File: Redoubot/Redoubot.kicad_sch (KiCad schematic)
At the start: 4 parts, among them U1 STM32G431RBTx, Y1 8MHz

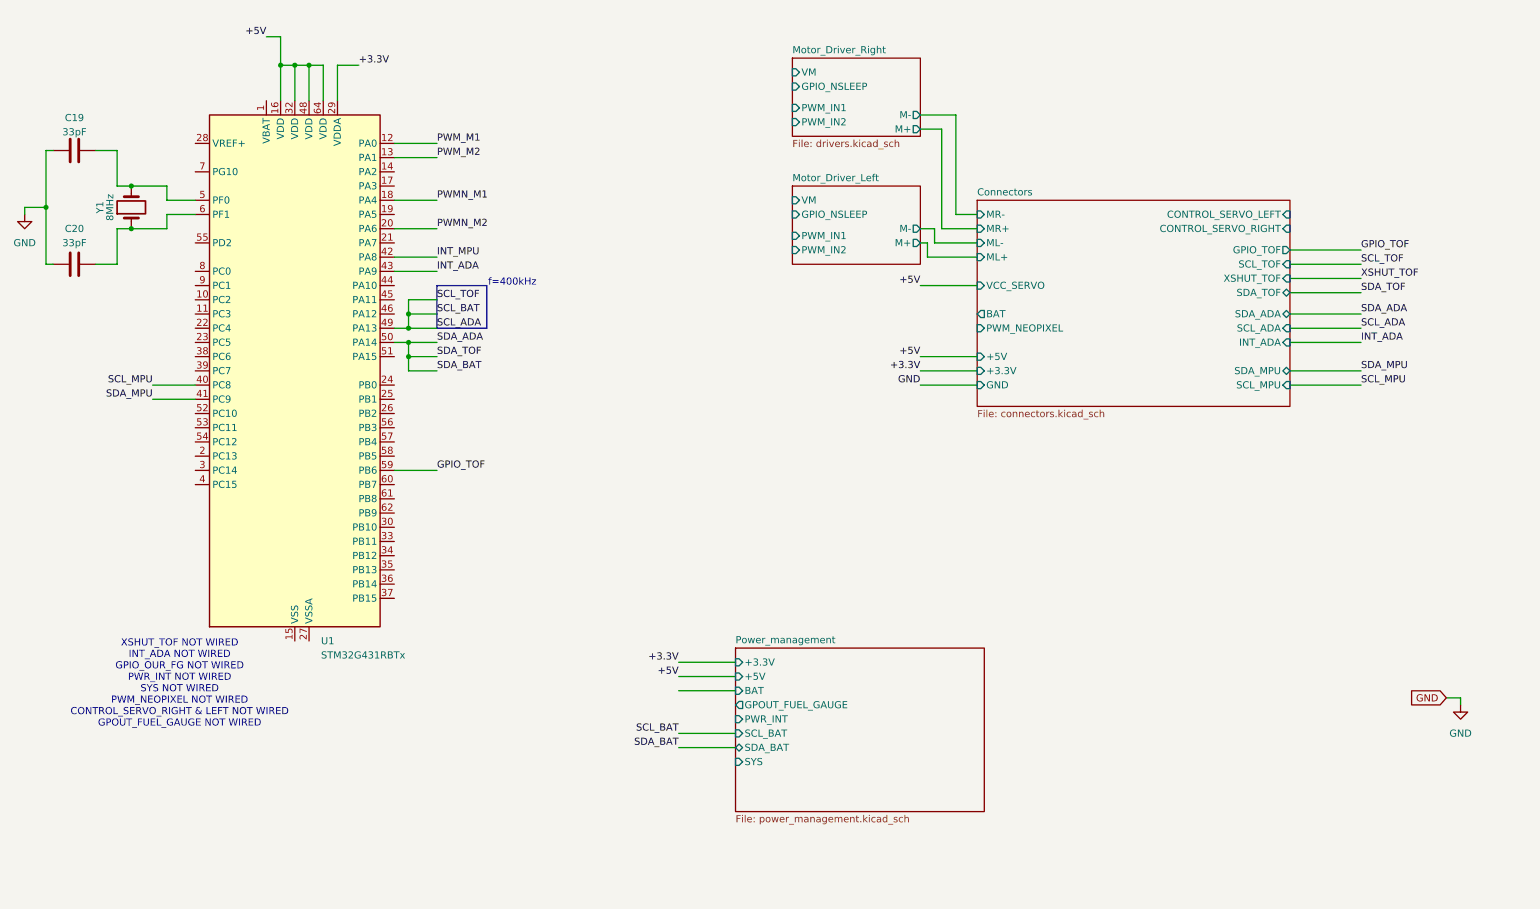
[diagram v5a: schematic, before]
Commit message: feat: added DFPlayer Mini and HM10 connectors
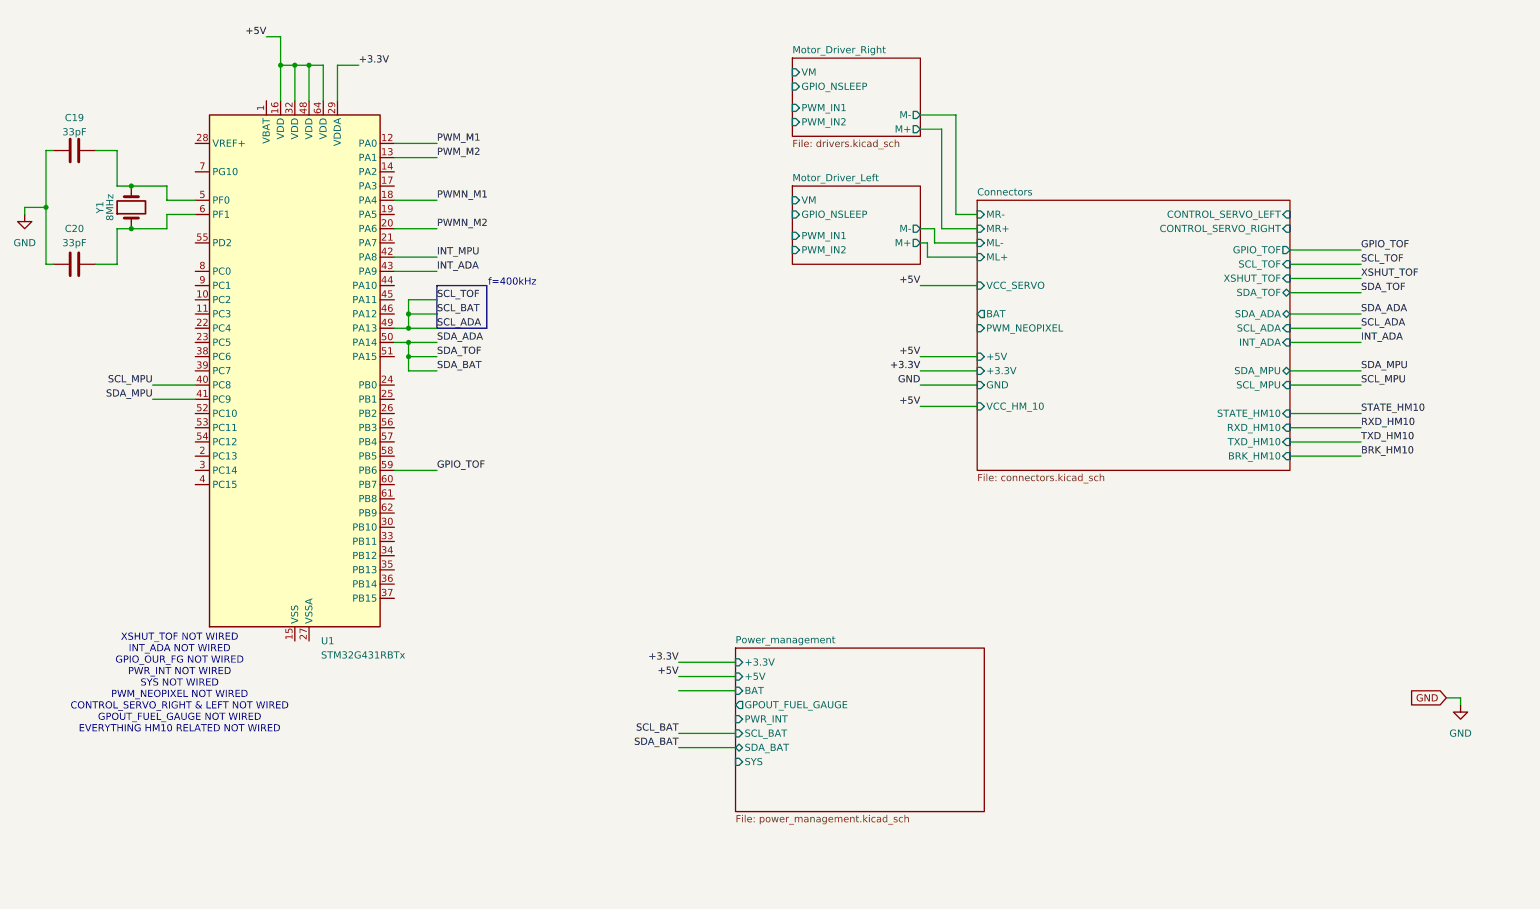
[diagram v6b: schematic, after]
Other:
- sheet Connectors ports: added BRK_HM10, RXD_HM10, STATE_HM10, TXD_HM10, VCC_HM_10; removed none
- note added: "XSHUT_TOF NOT WIRED INT_ADA NOT WIRED GPIO_OUR_FG NOT WIRED PWR_INT NOT WIRED SYS NOT WIRED PWM_NEOPIXEL NOT WIRED CONTROL_SERVO_RIGHT & LEFT NOT WIRED GPOUT_FUEL_GAUGE NOT WIRED EVERYTHING HM10 RELATED NOT WIRED"
- note removed: "XSHUT_TOF NOT WIRED INT_ADA NOT WIRED GPIO_OUR_FG NOT WIRED PWR_INT NOT WIRED SYS NOT WIRED PWM_NEOPIXEL NOT WIRED CONTROL_SERVO_RIGHT & LEFT NOT WIRED GPOUT_FUEL_GAUGE NOT WIRED"
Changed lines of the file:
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@@
 		)
 	)
-	(text "XSHUT_TOF NOT WIRED\nINT_ADA NOT WIRED\nGPIO_OUR_FG NOT WIRED\nPWR_INT NOT WIRED\nSYS NOT WIRED\nPWM_NEOPIXEL NOT WIRED\nCONTROL_SERVO_RIGHT & LEFT NOT WIRED\nGPOUT_FUEL_GAUGE NOT WIRED"
+	(text "XSHUT_TOF NOT WIRED\nINT_ADA NOT WIRED\nGPIO_OUR_FG NOT WIRED\nPWR_INT NOT WIRED\nSYS NOT WIRED\nPWM_NEOPIXEL NOT WIRED\nCONTROL_SERVO_RIGHT & LEFT NOT WIRED\nGPOUT_FUEL_GAUGE NOT WIRED\nEVERYTHING HM10 RELATED NOT WIRED\n"
 		(exclude_from_sim no)
 		(at 42.926 134.62 0)
@@
 	(wire
 		(pts
+			(xy 175.26 85.09) (xy 185.42 85.09)
+		)
+		(stroke
+			(width 0)
+			(type default)
+		)
+	)
+	(wire
+		(pts
+			(xy 241.3 86.36) (xy 254 86.36)
+		)
+		(stroke
+			(width 0)
+			(type default)
+		)
+	)
+	(wire
+		(pts
 			(xy 241.3 62.23) (xy 254 62.23)
 		)
@@
 	(wire
 		(pts
+			(xy 241.3 91.44) (xy 254 91.44)
+		)
+		(stroke
+			(width 0)
+			(type default)
+		)
+	)
+	(wire
+		(pts
 			(xy 241.3 68.58) (xy 254 68.58)
 		)
@@
 	(wire
 		(pts
+			(xy 241.3 93.98) (xy 254 93.98)
+		)
+		(stroke
+			(width 0)
+			(type default)
+		)
+	)
+	(wire
+		(pts
 			(xy 83.82 71.12) (xy 81.28 71.12)
 		)
@@
 		(pts
 			(xy 31.75 45.72) (xy 31.75 39.37)
+		)
+		(stroke
+			(width 0)
+			(type default)
+		)
+	)
+	(wire
+		(pts
+			(xy 241.3 88.9) (xy 254 88.9)
 		)
 		(stroke
@@
 		)
 	)
+	(label "TXD_HM10"
+		(at 254 91.44 0)
+		(effects
+			(font
+				(size 1.27 1.27)
+			)
+			(justify left bottom)
+		)
+	)
 	(label "SDA_ADA"
 		(at 88.9 73.66 0)
@@
 	)
 	(label "+5V"
+		(at 175.26 85.09 180)
+		(effects
+			(font
+				(size 1.27 1.27)
+			)
+			(justify right bottom)
+		)
+	)
+	(label "+5V"
 		(at 175.26 63.5 180)
 		(effects
@@
 		)
 	)
+	(label "STATE_HM10"
+		(at 254 86.36 0)
+		(effects
+			(font
+				(size 1.27 1.27)
+			)
+			(justify left bottom)
+		)
+	)
 	(label "SCL_BAT"
 		(at 132.08 143.51 180)
@@
 		)
 	)
+	(label "RXD_HM10"
+		(at 254 88.9 0)
+		(effects
+			(font
+				(size 1.27 1.27)
+			)
+			(justify left bottom)
+		)
+	)
 	(label "+3.3V"
 		(at 175.26 78.74 180)
@@
 	(label "PWM_M1"
 		(at 88.9 38.1 0)
+		(effects
+			(font
+				(size 1.27 1.27)
+			)
+			(justify left bottom)
+		)
+	)
+	(label "BRK_HM10"
+		(at 254 93.98 0)
 		(effects
 			(font
@@
 	(sheet
 		(at 185.42 48.26)
-		(size 55.88 36.83)
+		(size 55.88 48.26)
 		(exclude_from_sim no)
 		(in_bom yes)
@@
 		)
 		(property "Sheetfile" "connectors.kicad_sch"
-			(at 185.42 85.6746 0)
+			(at 185.42 97.1046 0)
 			(show_name no)
 			(do_not_autoplace no)
@@
 			)
 		)
+		(pin "BRK_HM10" input
+			(at 241.3 93.98 0)
+			(effects
+				(font
+					(size 1.27 1.27)
+				)
+				(justify right)
+			)
+		)
+		(pin "RXD_HM10" input
+			(at 241.3 88.9 0)
+			(effects
+				(font
+					(size 1.27 1.27)
+				)
+				(justify right)
+			)
+		)
+		(pin "STATE_HM10" input
+			(at 241.3 86.36 0)
+			(effects
+				(font
+					(size 1.27 1.27)
+				)
+				(justify right)
+			)
+		)
+		(pin "TXD_HM10" input
+			(at 241.3 91.44 0)
+			(effects
+				(font
+					(size 1.27 1.27)
+				)
+				(justify right)
+			)
+		)
+		(pin "VCC_HM_10" input
+			(at 185.42 85.09 180)
+			(effects
+				(font
+					(size 1.27 1.27)
+				)
+				(justify left)
+			)
+		)

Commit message: simply added the JLCPCB Part # as an LCSC field in the component descriptions
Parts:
- U1: LCSC (none) -> C431633
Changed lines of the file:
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@@
+			)
+		)
+		(property "LCSC" "C431633"
+			(at 63.5 78.74 0)
+			(hide yes)
+			(show_name no)
+			(do_not_autoplace no)
+			(effects
+				(font
+					(size 1.27 1.27)
+				)
 			)
 		)

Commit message: Added footprints for capacitors
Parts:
- C19, C20: footprint (none) -> Capacitor_SMD:C_0402_1005Metric
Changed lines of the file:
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@@
 			)
 		)
-		(property "Footprint" ""
+		(property "Footprint" "Capacitor_SMD:C_0402_1005Metric"
 			(at 27.94 58.7248 0)
 			(hide yes)
@@
 			)
 		)
-		(property "Footprint" ""
+		(property "Footprint" "Capacitor_SMD:C_0402_1005Metric"
 			(at 27.94 38.4048 0)
 			(hide yes)
